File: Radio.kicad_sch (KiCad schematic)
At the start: 0 parts

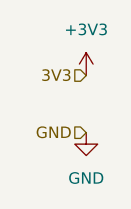
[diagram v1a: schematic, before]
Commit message: Updated heiarchal power labels
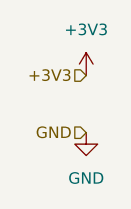
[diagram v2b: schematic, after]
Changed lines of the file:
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@@
 		(comment 1 "Victoria Pacheco")
 	)
-	(hierarchical_label "3V3"
+	(hierarchical_label "+3V3"
 		(shape input)
 		(at 38.1 38.1 180)

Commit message: Merged radio
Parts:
- added AE1: Antenna_Shield, symbol Device:Antenna_Shield
- added C?: 0.1uF, symbol Device:C_Small
- added C?: 10uF, symbol Device:C_Small
- added U?: RFM69HCW, VSSOP10_DGS_TEX, symbol Avionics_Symbols:INA229AQDGSRQ1
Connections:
- net +3V3: now also C?.1, C?.1, U?.13 (3.3V)
- net GND: now also AE1.2 (Shield), C?.2, C?.2, U?.1 (GND), U?.10 (GND), U?.8 (GND)
- new net: AE1.1 (A), U?.9 (ANT)
- new net CS_RADIO: U?.5 (NSS)
- new net INT_RADIO: U?.14 (DIO0)
- new net MISO: U?.2 (MISO)
- new net MOSI: U?.3 (MOSI)
- new net RST_RADIO: U?.6 (RESET)
- new net SCK: U?.4 (SCK)
- no-connect marks 0 -> 5

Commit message: Radio footprint selection
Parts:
- removed C?: 0.1uF, symbol Device:C_Small
- removed C?: 10uF, symbol Device:C_Small
- removed U?: RFM69HCW, VSSOP10_DGS_TEX, symbol Avionics_Symbols:INA229AQDGSRQ1
- added C15: 10uF, Capacitor_SMD:C_0603_1608Metric, symbol Device:C_Small
- added C16: 0.1uF, Capacitor_SMD:C_0603_1608Metric, symbol Device:C_Small
- added U5: RFM69HCW, RF_Module:HOPERF_RFM9XW_SMD, symbol Avionics_Symbols:INA229AQDGSRQ1
- AE1: footprint (none) -> Connector_Coaxial:SMA_Samtec_SMA-J-P-H-ST-EM1_EdgeMount
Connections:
- net +3V3: now also C15.1, C16.1, U5.13 (3.3V)
- net CS_RADIO: now also U5.5 (NSS)
- net GND: now also C15.2, C16.2, U5.1 (GND), U5.10 (GND), U5.8 (GND)
- net INT_RADIO: now also U5.14 (DIO0)
- net MISO: now also U5.2 (MISO)
- net MOSI: now also U5.3 (MOSI)
- net RST_RADIO: now also U5.6 (RESET)
- net SCK: now also U5.4 (SCK)
- net at AE1.1 (A): now also U5.9 (ANT)

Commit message: Addeed part numbers
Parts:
- AE1: LCSC (none) -> C5199907
- C15: LCSC (none) -> C96446
- C16: LCSC (none) -> C14663
- U5: LCSC (none) -> C2844474
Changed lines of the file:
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@@
+			)
+		)
+		(property "LCSC" "C5199907"
+			(at 135.89 62.23 90)
+			(effects
+				(font
+					(size 1.27 1.27)
+				)
+				(hide yes)
 			)
 		)
@@
 			)
 		)
+		(property "LCSC" "C2844474"
+			(at 106.68 67.31 0)
+			(effects
+				(font
+					(size 1.27 1.27)
+				)
+				(hide yes)
+			)
+		)
 		(pin "3"
 		)
@@
 			)
 		)
+		(property "LCSC" "C14663"
+			(at 71.12 72.39 0)
+			(effects
+				(font
+					(size 1.27 1.27)
+				)
+				(hide yes)
+			)
+		)
 		(pin "1"
 		)
@@
 			(at 63.5 72.39 0)
 			(effects
+				(font
+					(size 1.27 1.27)
+				)
+				(hide yes)
+			)
+		)
+		(property "LCSC" "C96446"
+			(at 63.5 72.39 0)
+			(effects

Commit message: Added Digikey Components
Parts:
- AE1: Digikey (none) -> 142-0701-801
- U5: Digikey (none) -> 1568-13909-ND
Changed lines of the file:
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@@
+			)
+		)
+		(property "Digikey" "142-0701-801"
+			(at 135.89 62.23 90)
+			(effects
+				(font
+					(size 1.27 1.27)
+				)
+				(hide yes)
 			)
 		)
@@
 			)
 		)
+		(property "Digikey" "1568-13909-ND"
+			(at 106.68 67.31 0)
+			(effects
+				(font
+					(size 1.27 1.27)
+				)
+				(hide yes)
+			)
+		)
 		(pin "3"
 		)
@@
 			)
 		)
+		(property "Digikey" ""
+			(at 71.12 72.39 0)
+			(effects
+				(font
+					(size 1.27 1.27)
+				)
+				(hide yes)
+			)
+		)
 		(pin "1"
 		)
@@
 			(at 63.5 72.39 0)
 			(effects
+				(font
+					(size 1.27 1.27)
+				)
+				(hide yes)
+			)
+		)
+		(property "Digikey" ""
+			(at 63.5 72.39 0)
+			(effects
